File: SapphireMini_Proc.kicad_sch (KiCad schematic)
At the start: 61 parts, among them J801 Conn_02x05_Odd_Even, J802 Conn_02x05_Odd_Even, J803 Conn_01x08_Female, J804 Conn_01x04_Male, J805 USB_B_Micro, SW801 EVQP7C01P, U801 ATSAMD21G18A-A

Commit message: Corrected to get clean review on schematic
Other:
- company: Southern Methodist Univ -> (none)
- title: Sapphire Mini M2 -> (none)
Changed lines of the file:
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@@
 (kicad_sch (version 20211123) (generator eeschema)
   (paper "A4")
-  (title_block
-    (title "Sapphire Mini M2")
-    (date "2022-09-26")
-    (rev "1")
-    (company "Southern Methodist Univ")
-    (comment 1 "Chris Hayward")
-  )
   (junction (at 170.18 44.45) (diameter 0) (color 0 0 0 0)
   )
@@
   (symbol (lib_id "power:GND") (at 162.56 185.42 0) (unit 1)
     (in_bom yes) (on_board yes)
-    (property "Reference" "#PWR0809" (id 0) (at 162.56 191.77 0)
+    (property "Reference" "#PWR?" (id 0) (at 162.56 191.77 0)
       (effects (font (size 1.27 1.27)) hide)
     )
@@
   (symbol (lib_id "power:GND") (at 132.08 69.85 0) (unit 1)
     (in_bom yes) (on_board yes)
-    (property "Reference" "#PWR0811" (id 0) (at 132.08 76.2 0)
+    (property "Reference" "#PWR?" (id 0) (at 132.08 76.2 0)
       (effects (font (size 1.27 1.27)) hide)
     )
@@
   (symbol (lib_id "power:GNDA") (at 213.36 67.31 0) (unit 1)
     (in_bom yes) (on_board yes)
-    (property "Reference" "#PWR0812" (id 0) (at 213.36 73.66 0)
+    (property "Reference" "#PWR?" (id 0) (at 213.36 73.66 0)
       (effects (font (size 1.27 1.27)) hide)
     )
@@
   (symbol (lib_id "power:GNDA") (at 165.1 185.42 0) (unit 1)
     (in_bom yes) (on_board yes)
-    (property "Reference" "#PWR0810" (id 0) (at 165.1 191.77 0)
+    (property "Reference" "#PWR?" (id 0) (at 165.1 191.77 0)
       (effects (font (size 1.27 1.27)) hide)
     )
@@
   (symbol (lib_id "power:GND") (at 146.05 58.42 0) (unit 1)
     (in_bom yes) (on_board yes)
-    (property "Reference" "#PWR0808" (id 0) (at 146.05 64.77 0)
+    (property "Reference" "#PWR?" (id 0) (at 146.05 64.77 0)
       (effects (font (size 1.27 1.27)) hide)
     )
@@
   (symbol (lib_id "power:GND") (at 64.77 62.23 0) (unit 1)
     (in_bom yes) (on_board yes)
-    (property "Reference" "#PWR0803" (id 0) (at 64.77 68.58 0)
+    (property "Reference" "#PWR?" (id 0) (at 64.77 68.58 0)
       (effects (font (size 1.27 1.27)) hide)
     )
@@
   (symbol (lib_id "power:GNDA") (at 73.66 88.9 0) (unit 1)
     (in_bom yes) (on_board yes)
-    (property "Reference" "#PWR0806" (id 0) (at 73.66 95.25 0)
+    (property "Reference" "#PWR?" (id 0) (at 73.66 95.25 0)
       (effects (font (size 1.27 1.27)) hide)
     )
@@
   (symbol (lib_id "power:GND") (at 64.77 77.47 0) (unit 1)
     (in_bom yes) (on_board yes)
-    (property "Reference" "#PWR0804" (id 0) (at 64.77 83.82 0)
+    (property "Reference" "#PWR?" (id 0) (at 64.77 83.82 0)
       (effects (font (size 1.27 1.27)) hide)
     )
@@
   (symbol (lib_id "power:GND") (at 64.77 92.71 0) (unit 1)
     (in_bom yes) (on_board yes)
-    (property "Reference" "#PWR0805" (id 0) (at 64.77 99.06 0)
+    (property "Reference" "#PWR?" (id 0) (at 64.77 99.06 0)
       (effects (font (size 1.27 1.27)) hide)
     )
@@
   (symbol (lib_id "power:GND") (at 25.4 166.37 0) (mirror y) (unit 1)
     (in_bom yes) (on_board yes)
-    (property "Reference" "#PWR0801" (id 0) (at 25.4 172.72 0)
+    (property "Reference" "#PWR?" (id 0) (at 25.4 172.72 0)
       (effects (font (size 1.27 1.27)) hide)
     )
@@
   (symbol (lib_id "power:GND") (at 48.26 132.08 0) (unit 1)
     (in_bom yes) (on_board yes)
-    (property "Reference" "#PWR0802" (id 0) (at 48.26 138.43 0)
+    (property "Reference" "#PWR?" (id 0) (at 48.26 138.43 0)
       (effects (font (size 1.27 1.27)) hide)
     )
@@
   (symbol (lib_id "power:GND") (at 226.06 29.21 0) (mirror y) (unit 1)
     (in_bom yes) (on_board yes)
-    (property "Reference" "#PWR0813" (id 0) (at 226.06 35.56 0)
+    (property "Reference" "#PWR?" (id 0) (at 226.06 35.56 0)
       (effects (font (size 1.27 1.27)) hide)
     )
@@
   (symbol (lib_id "power:GND") (at 232.41 43.18 0) (mirror y) (unit 1)
     (in_bom yes) (on_board yes)
-    (property "Reference" "#PWR0814" (id 0) (at 232.41 49.53 0)
+    (property "Reference" "#PWR?" (id 0) (at 232.41 49.53 0)
       (effects (font (size 1.27 1.27)) hide)
     )
@@
   (symbol (lib_id "power:GND") (at 234.95 92.71 0) (unit 1)
     (in_bom yes) (on_board yes)
-    (property "Reference" "#PWR0815" (id 0) (at 234.95 99.06 0)
-      (effects (font (size 1.27 1.27)) hide)
-    )
+    (property "Reference" "#PWR?" (id 0) (at 234.95 99.06 0)
+      (effects (font (size 1.27 1.27)) hide)
+    )

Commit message: Minor changes to annotation
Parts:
- renumbered C808 to C804, C810 to C805, C804 to C806, C805 to C807, C806 to C808, C807 to C809, C809 to C810, J805 to J801, J801 to J802, J802 to J803, J803 to J804, J804 to J805, R811 to R807, R813 to R808, R807 to R809, R812 to R811, R814 to R812, R815 to R813, R816 to R814, R817 to R815, R818 to R816, R819 to R817, R820 to R818, R821 to R819, R822 to R820, R823 to R821, R824 to R822, R825 to R823, R826 to R824, R827 to R825, R828 to R826, R829 to R827, R830 to R828, R831 to R829, R832 to R830, R833 to R831, R834 to R832, R835 to R833, R836 to R834, R837 to R835, R838 to R836, R840 to R837, R841 to R838

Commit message: daily update
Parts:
- added R839, R840, R841, R842: 47, Resistor_SMD:R_0603_1608Metric, symbol Device:R_US
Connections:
- net 32KHz: now also R839.2; no longer U801.1 (PA00)
- net I2C_SCL: now also R842.2; no longer U801.32 (PA23)
- net I2C_SDA: now also R841.2; no longer U801.31 (PA22)
- net SPI_MISO: now also R840.2; no longer U801.28 (PA19)
- new net: R839.1, U801.1 (PA00)
- new net: R840.1, U801.28 (PA19)
- new net: R841.1, U801.31 (PA22)
- new net: R842.1, U801.32 (PA23)
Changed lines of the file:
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@@
     (stroke (width 0) (type default) (color 0 0 0 0))
   )
-  (wire (pts (xy 144.78 80.01) (xy 96.52 80.01))
+  (wire (pts (xy 144.78 80.01) (xy 143.51 80.01))
     (stroke (width 0) (type default) (color 0 0 0 0))
   )
@@
     (stroke (width 0) (type default) (color 0 0 0 0))
   )
+  (wire (pts (xy 135.89 135.89) (xy 96.52 135.89))
+    (stroke (width 0) (type default) (color 0 0 0 0))
+  )
   (wire (pts (xy 43.18 74.93) (xy 30.48 74.93))
     (stroke (width 0) (type default) (color 0 0 0 0))
@@
     (stroke (width 0) (type default) (color 0 0 0 0))
   )
-  (wire (pts (xy 144.78 120.65) (xy 96.52 120.65))
+  (wire (pts (xy 96.52 120.65) (xy 144.78 120.65))
     (stroke (width 0) (type default) (color 0 0 0 0))
   )
@@
     (stroke (width 0) (type default) (color 0 0 0 0))
   )
-  (wire (pts (xy 144.78 128.27) (xy 96.52 128.27))
+  (wire (pts (xy 144.78 128.27) (xy 143.51 128.27))
     (stroke (width 0) (type default) (color 0 0 0 0))
   )
@@
     (stroke (width 0) (type default) (color 0 0 0 0))
   )
+  (wire (pts (xy 135.89 128.27) (xy 96.52 128.27))
+    (stroke (width 0) (type default) (color 0 0 0 0))
+  )
   (wire (pts (xy 226.06 16.51) (xy 232.41 16.51))
     (stroke (width 0) (type default) (color 0 0 0 0))
@@
     (stroke (width 0) (type default) (color 0 0 0 0))
   )
+  (wire (pts (xy 135.89 80.01) (xy 96.52 80.01))
+    (stroke (width 0) (type default) (color 0 0 0 0))
+  )
   (wire (pts (xy 35.56 140.97) (xy 74.93 140.97))
     (stroke (width 0) (type default) (color 0 0 0 0))
@@
     (stroke (width 0) (type default) (color 0 0 0 0))
   )
+  (wire (pts (xy 135.89 138.43) (xy 96.52 138.43))
+    (stroke (width 0) (type default) (color 0 0 0 0))
+  )
   (wire (pts (xy 153.67 67.31) (xy 154.94 68.58))
     (stroke (width 0) (type default) (color 0 0 0 0))
@@
     (stroke (width 0) (type default) (color 0 0 0 0))
   )
-  (wire (pts (xy 144.78 138.43) (xy 96.52 138.43))
+  (wire (pts (xy 144.78 138.43) (xy 143.51 138.43))
     (stroke (width 0) (type default) (color 0 0 0 0))
   )
@@
     (stroke (width 0) (type default) (color 0 0 0 0))
   )
-  (wire (pts (xy 144.78 135.89) (xy 96.52 135.89))
+  (wire (pts (xy 144.78 135.89) (xy 143.51 135.89))
     (stroke (width 0) (type default) (color 0 0 0 0))
   )
@@
     (pin "9")
   )
+  (symbol (lib_id "Device:R_US") (at 139.7 128.27 270) (unit 1)
+    (in_bom yes) (on_board yes)
+    (property "Reference" "R840" (id 0) (at 135.89 127 90))
+    (property "Value" "47" (id 1) (at 142.24 127 90))
+    (property "Footprint" "Resistor_SMD:R_0603_1608Metric" (id 2) (at 139.446 129.286 90)
+      (effects (font (size 1.27 1.27)) hide)
+    )
+    (property "Datasheet" "~" (id 3) (at 139.7 128.27 0)
+      (effects (font (size 1.27 1.27)) hide)
+    )
+    (pin "1")
+    (pin "2")
+  )
+  (symbol (lib_id "Device:R_US") (at 139.7 135.89 270) (unit 1)
+    (in_bom yes) (on_board yes)
+    (property "Reference" "R841" (id 0) (at 135.89 134.62 90))
+    (property "Value" "47" (id 1) (at 142.24 134.62 90))
+    (property "Footprint" "Resistor_SMD:R_0603_1608Metric" (id 2) (at 139.446 136.906 90)
+      (effects (font (size 1.27 1.27)) hide)
+    )
+    (property "Datasheet" "~" (id 3) (at 139.7 135.89 0)
+      (effects (font (size 1.27 1.27)) hide)
+    )
+    (pin "1")
+    (pin "2")
+  )
   (symbol (lib_id "power:PWR_FLAG") (at 160.02 48.26 270) (unit 1)
     (in_bom yes) (on_board yes)
@@
     )
     (pin "1")
+  )
+  (symbol (lib_id "Device:R_US") (at 139.7 80.01 270) (unit 1)
+    (in_bom yes) (on_board yes)
+    (property "Reference" "R839" (id 0) (at 135.89 78.74 90))
+    (property "Value" "47" (id 1) (at 142.24 78.74 90))
+    (property "Footprint" "Resistor_SMD:R_0603_1608Metric" (id 2) (at 139.446 81.026 90)
+      (effects (font (size 1.27 1.27)) hide)
+    )
+    (property "Datasheet" "~" (id 3) (at 139.7 80.01 0)
+      (effects (font (size 1.27 1.27)) hide)
+    )
+    (pin "1")
+    (pin "2")
   )
   (symbol (lib_id "Device:C") (at 156.21 30.48 270) (unit 1)
@@
       (effects (font (size 1.27 1.27)) hide)
     )
+    (pin "1")
+    (pin "2")
+  )
+  (symbol (lib_id "Device:R_US") (at 139.7 138.43 270) (unit 1)
+    (in_bom yes) (on_board yes)
+    (property "Reference" "R842" (id 0) (at 135.89 137.16 90))
+    (property "Value" "47" (id 1) (at 142.24 137.16 90))
+    (property "Footprint" "Resistor_SMD:R_0603_1608Metric" (id 2) (at 139.446 139.446 90)
+      (effects (font (size 1.27 1.27)) hide)
+    )
+    (property "Datasheet" "~" (id 3) (at 139.7 138.43 0)
+      (effects (font (size 1.27 1.27)) hide)
+    )

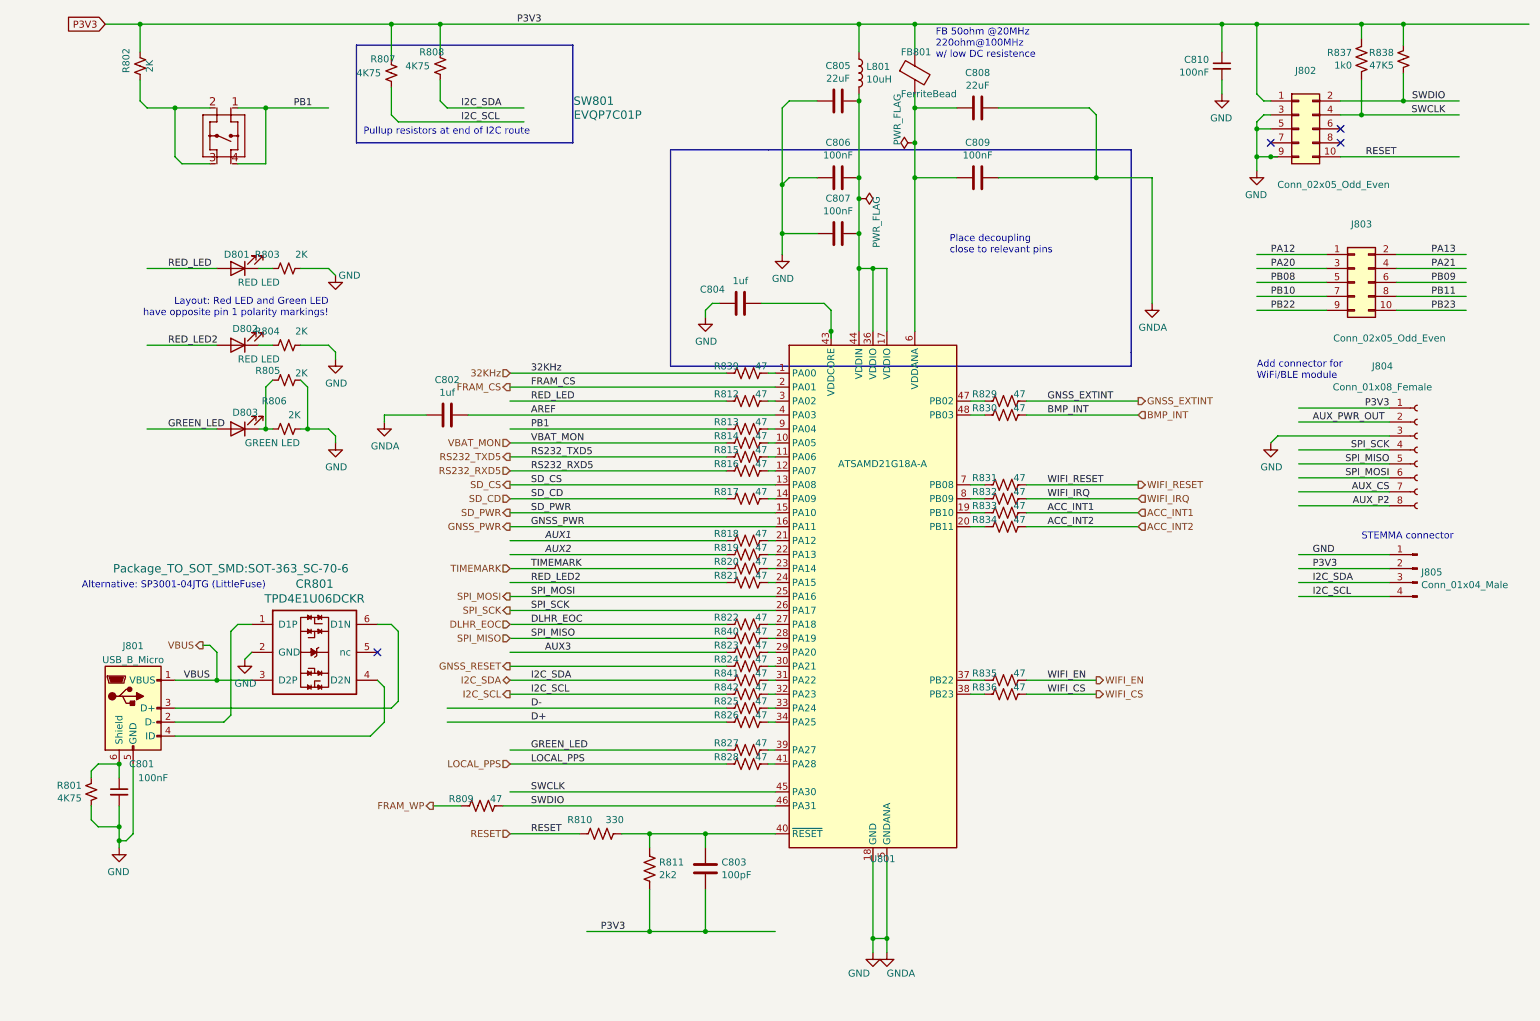
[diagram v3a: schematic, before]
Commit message: Footprints complete. Starting layout
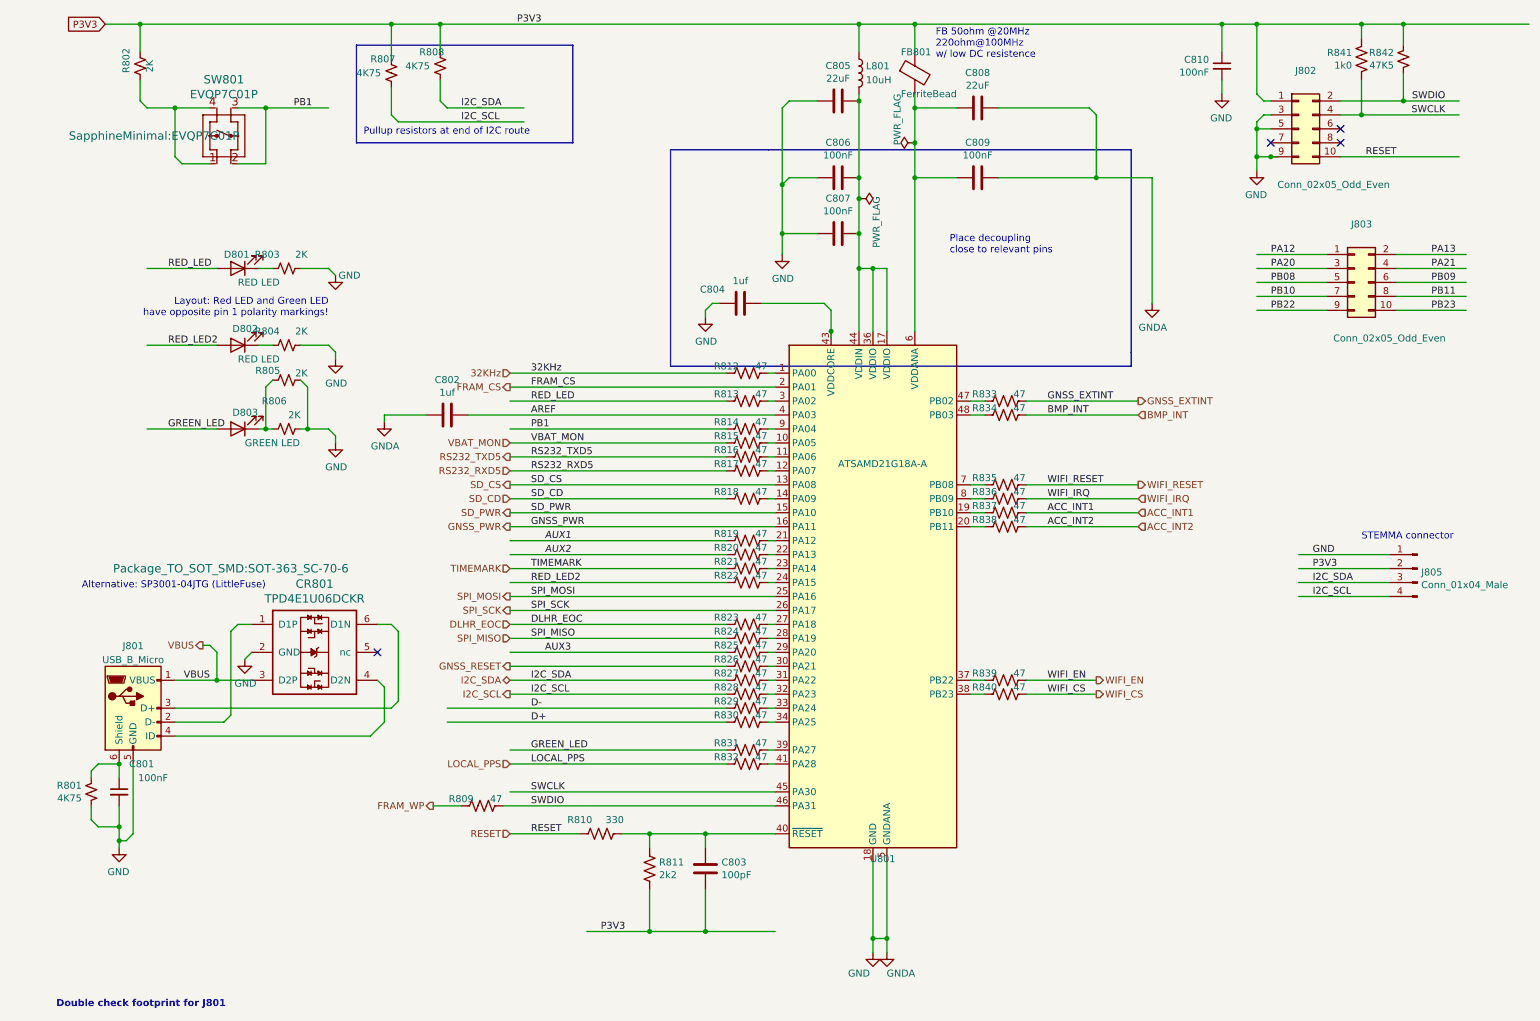
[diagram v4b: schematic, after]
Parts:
- removed J804: Conn_01x08_Female, Connector_PinSocket_2.54mm:PinSocket_1x08_P2.54mm_Vertical, symbol Connector:Conn_01x08_Female
- C801, C810: MPN CL10B104KA8NNNC -> CL05A104KA5NNNC
- C802, C804: MPN (none) -> CL21B105KOFNNNG; Manufacturer (none) -> Samsung; Populate (none) -> 1
- C803: MPN (none) -> CL10C391JB81PNC
- C805, C808: MPN (none) -> CL21A226MAYNNNE; Manufacturer (none) -> Samsung; Populate (none) -> 1
- C806, C807, C809: MPN (none) -> CL05A104KA5NNNC; Manufacturer (none) -> Samsung; Populate (none) -> 1
- CR801, J805: Status MiniReel -> (none)
- D801, D802, D803: Status CutTape -> (none)
- FB801: footprint (none) -> Inductor_SMD:L_0201_0603Metric; MPN (none) -> BLM18AG221SN1D
- J801: footprint (none) -> SapphineMinimal:uUSB_B; MPN (none) -> 10118193-0001LF; Manufacturer (none) -> MOLEX
- L801: footprint (none) -> SapphineMinimal:NR3012T100M; MPN (none) -> NR3012T100M; Manufacturer (none) -> Taiyo Yuden
- SW801: footprint EVQP7C/L_PAN -> SapphineMinimal:EVQP7C01P
- U801: MPN (none) -> ATSAMD21G18A-AUT; Manufacturer (none) -> Microchip Technology
- renumbered R839 to R812, R812 to R813, R813 to R814, R814 to R815, R815 to R816, R816 to R817, R817 to R818, R818 to R819, R819 to R820, R820 to R821, R821 to R822, R822 to R823, R840 to R824, R823 to R825, R824 to R826, R841 to R827, R842 to R828, R825 to R829, R826 to R830, R827 to R831, R828 to R832, R829 to R833, R830 to R834, R831 to R835, R832 to R836, R833 to R837, R834 to R838, R835 to R839, R836 to R840, R837 to R841, R838 to R842
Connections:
- net PB1: now also SW801.2, SW801.3; no longer SW801.1, SW801.4
- new net: R802.2, SW801.1, SW801.4
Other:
- note added: "Double check footprint for J801"
- note removed: "Add connector for WiFi/BLE module"
